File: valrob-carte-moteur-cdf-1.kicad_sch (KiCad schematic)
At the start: 45 parts, among them J1 Conn_01x04_Pin, J2 Conn_01x02, J3 Conn_01x02, J4 USB_C_Receptacle_USB2.0_14P, J5 Conn_01x08, J6 Conn_01x08, J7 Conn_01x02, J8 Conn_01x02, SW1 SW_Push, SW2 SW_Push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

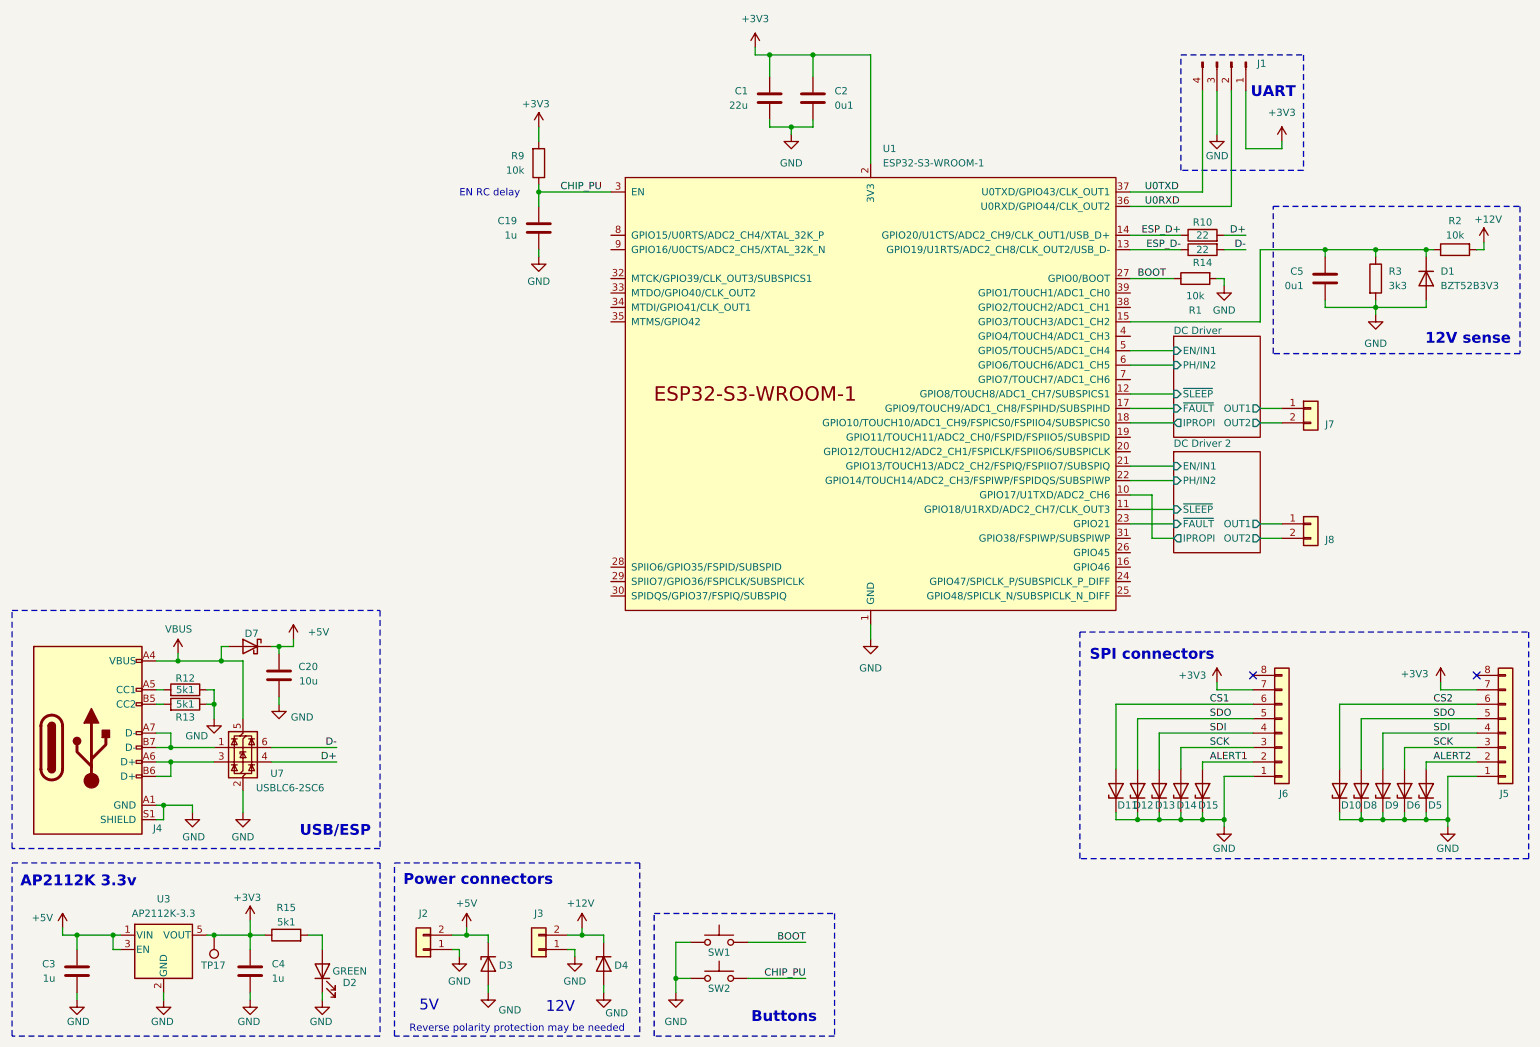
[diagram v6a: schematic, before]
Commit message: schem: connect SPI connectors to ESP32S3
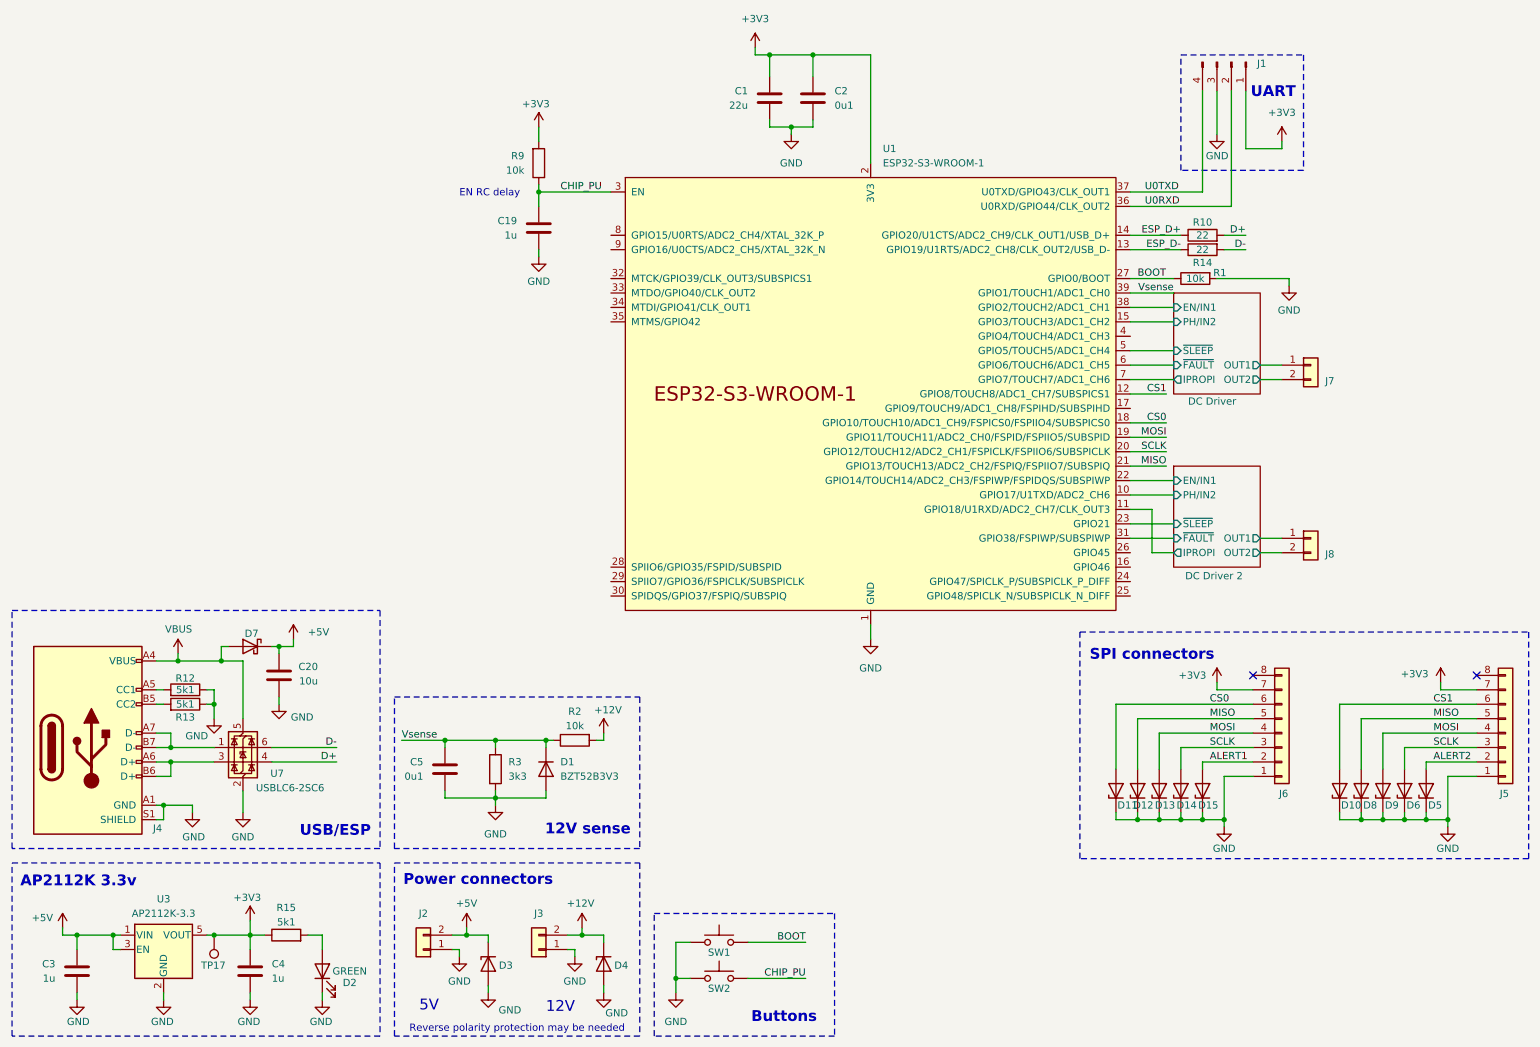
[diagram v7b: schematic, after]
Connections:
- net CS2 is gone; now on net CS1: D10.2 (A), J5.6 (Pin_6)
- net SCK is gone; now on net SCLK: D14.2 (A), D6.2 (A), J5.3 (Pin_3), J6.3 (Pin_3)
- net SDI is gone; now on net MOSI: D13.2 (A), D9.2 (A), J5.4 (Pin_4), J6.4 (Pin_4)
- net CS1: now also U1.12 (GPIO8/TOUCH8/ADC1_CH7/SUBSPICS1); no longer D11.2 (A), J6.6 (Pin_6)
- net DC Driver 2/EN/IN1: now also U1.22 (GPIO14/TOUCH14/ADC2_CH3/FSPIWP/FSPIDQS/SUBSPIWP); no longer U1.21 (GPIO13/TOUCH13/ADC2_CH2/FSPIQ/FSPIIO7/SUBSPIQ)
- net DC Driver 2/IPROPI: now also U1.11 (GPIO18/U1RXD/ADC2_CH7/CLK_OUT3); no longer U1.10 (GPIO17/U1TXD/ADC2_CH6)
- net DC Driver 2/PH/IN2: now also U1.10 (GPIO17/U1TXD/ADC2_CH6); no longer U1.22 (GPIO14/TOUCH14/ADC2_CH3/FSPIWP/FSPIDQS/SUBSPIWP)
- net DC Driver 2/~{FAULT}: now also U1.31 (GPIO38/FSPIWP/SUBSPIWP); no longer U1.23 (GPIO21)
- net DC Driver 2/~{SLEEP}: now also U1.23 (GPIO21); no longer U1.11 (GPIO18/U1RXD/ADC2_CH7/CLK_OUT3)
- net DC Driver/EN/IN1: now also U1.38 (GPIO2/TOUCH2/ADC1_CH1); no longer U1.5 (GPIO5/TOUCH5/ADC1_CH4)
- net DC Driver/IPROPI: now also U1.7 (GPIO7/TOUCH7/ADC1_CH6); no longer U1.18 (GPIO10/TOUCH10/ADC1_CH9/FSPICS0/FSPIIO4/SUBSPICS0)
- net DC Driver/PH/IN2: now also U1.15 (GPIO3/TOUCH3/ADC1_CH2); no longer U1.6 (GPIO6/TOUCH6/ADC1_CH5)
- net DC Driver/~{FAULT}: now also U1.6 (GPIO6/TOUCH6/ADC1_CH5); no longer U1.17 (GPIO9/TOUCH9/ADC1_CH8/FSPIHD/SUBSPIHD)
- net DC Driver/~{SLEEP}: now also U1.5 (GPIO5/TOUCH5/ADC1_CH4); no longer U1.12 (GPIO8/TOUCH8/ADC1_CH7/SUBSPICS1)
- net Vsense: now reaches C5.1, D1.1 (K), R2.1, R3.1
- net Vsense: now also U1.39 (GPIO1/TOUCH1/ADC1_CH0); no longer U1.15 (GPIO3/TOUCH3/ADC1_CH2)
- net MOSI: now reaches U1.19 (GPIO11/TOUCH11/ADC2_CH0/FSPID/FSPIIO5/SUBSPID)
- net SCLK: now reaches U1.20 (GPIO12/TOUCH12/ADC2_CH1/FSPICLK/FSPIIO6/SUBSPICLK)
- net SDO renamed MISO
- net MISO: now also U1.21 (GPIO13/TOUCH13/ADC2_CH2/FSPIQ/FSPIIO7/SUBSPIQ)
- new net CS0: D11.2 (A), J6.6 (Pin_6), U1.18 (GPIO10/TOUCH10/ADC1_CH9/FSPICS0/FSPIIO4/SUBSPICS0)
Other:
- moved on the sheet: C5, D1, J8, R2, R3

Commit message: schem: add various test points
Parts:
- added TP1, TP2, TP3: TestPoint, TestPoint:TestPoint_Pad_D2.0mm, symbol Connector:TestPoint
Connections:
- net +12V: now also TP2.1
- net +5V: now also TP1.1
- net Vsense: now also TP3.1
